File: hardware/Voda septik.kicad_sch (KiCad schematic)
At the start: 40 parts, among them J1 Screw_Terminal_01x09, J3 Display TM1637, J4 Display LCD I2C, J6 Screw_Terminal_01x09, U1 ESP32-DevKitC, U2 DC-DC 24V -> 5V, U3 ADS1115IDGS, U4 MAX3485-modul

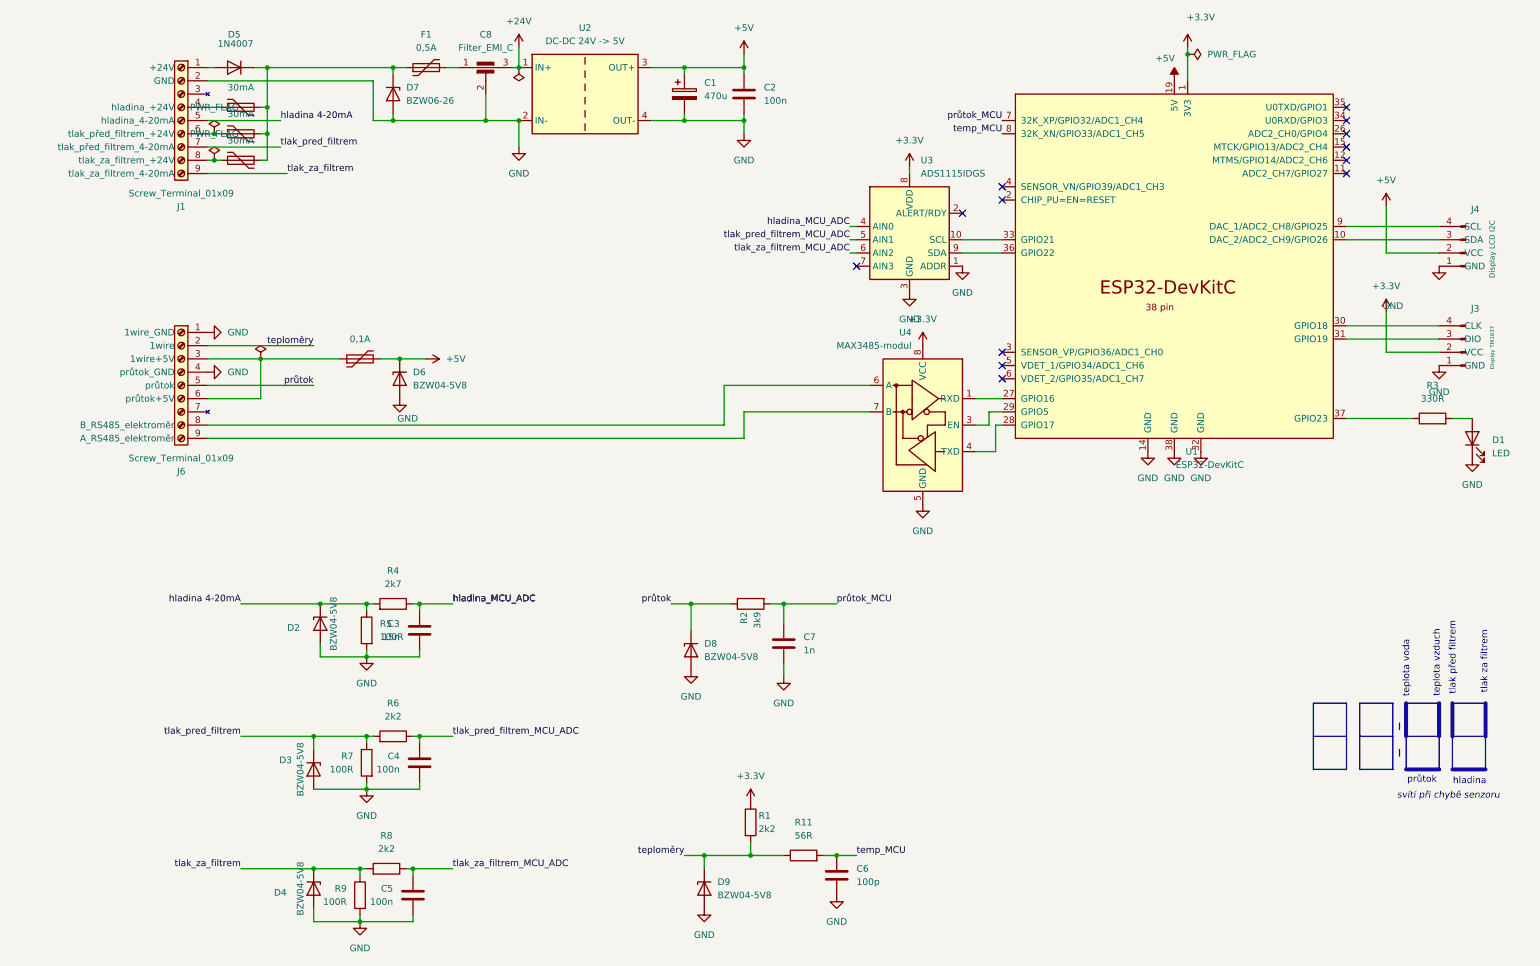
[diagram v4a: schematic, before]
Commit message: Vyvéjíme PCB a jsme v v koncích díky malé krabičce.
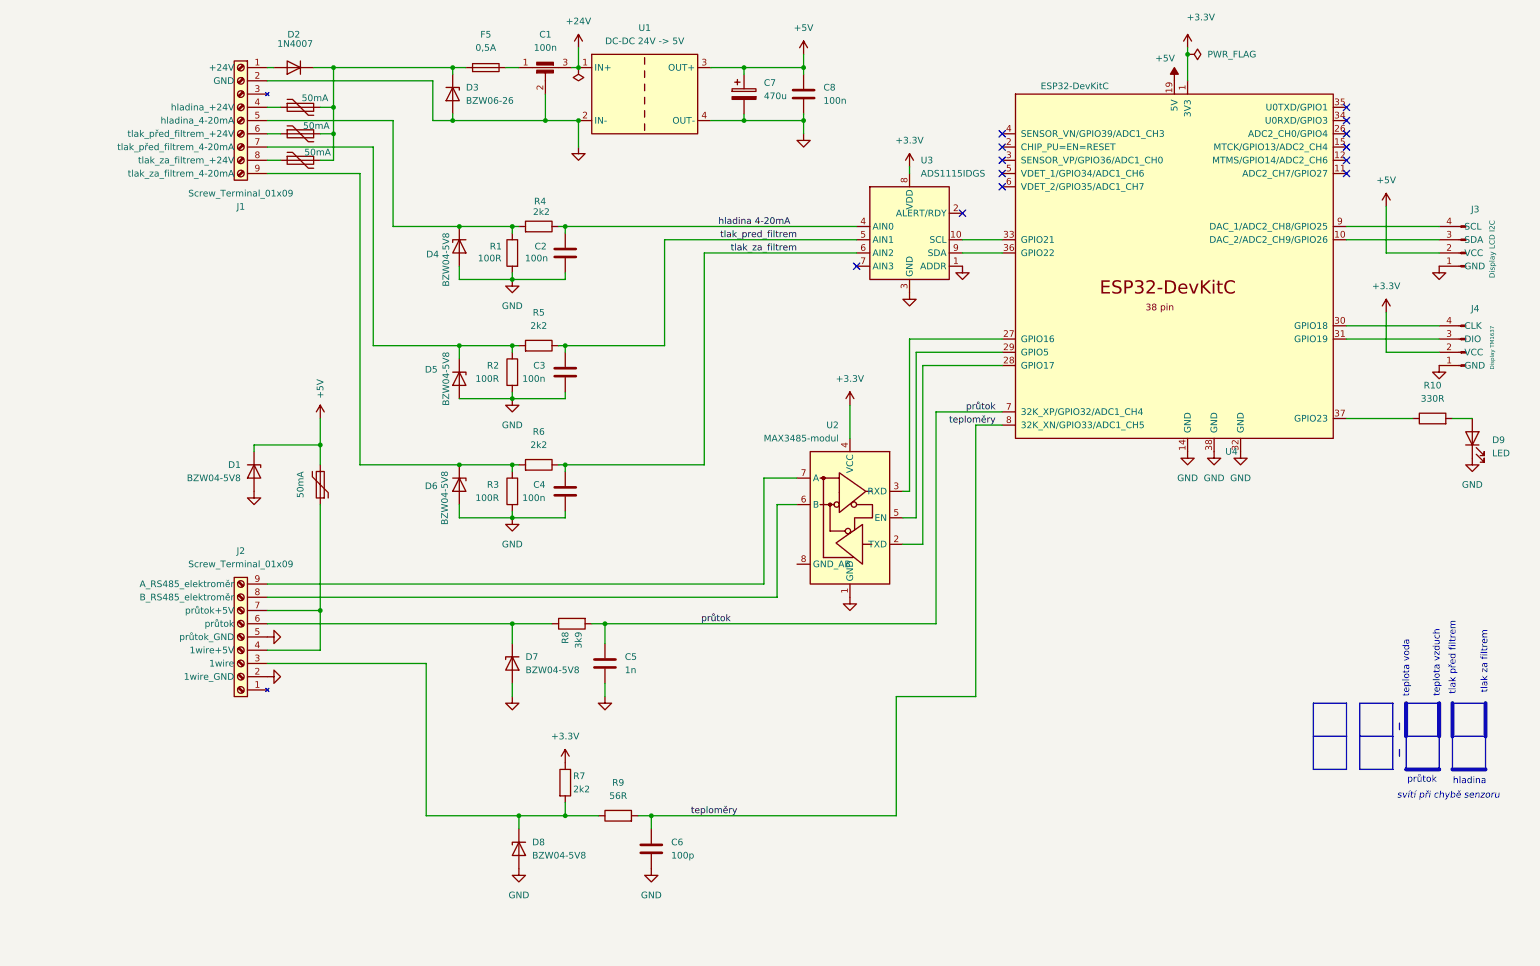
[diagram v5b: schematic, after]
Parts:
- C1: renamed from C8; value Filter_EMI_C -> 100n; footprint (none) -> martin:Odruseni_3x_2.54mm
- C2: renamed from C3; value 15n -> 100n; footprint (none) -> Capacitor_THT:C_Disc_D5.0mm_W2.5mm_P5.00mm
- C3: renamed from C4; footprint (none) -> Capacitor_THT:C_Disc_D5.0mm_W2.5mm_P5.00mm
- C4: renamed from C5; footprint (none) -> Capacitor_THT:C_Disc_D5.0mm_W2.5mm_P5.00mm
- C5: renamed from C7; footprint (none) -> Capacitor_THT:C_Disc_D5.0mm_W2.5mm_P5.00mm
- C6: footprint (none) -> Capacitor_THT:C_Disc_D5.0mm_W2.5mm_P5.00mm
- C7: renamed from C1; footprint (none) -> Capacitor_THT:CP_Radial_D10.0mm_P5.00mm
- C8: renamed from C2; footprint (none) -> Capacitor_THT:C_Disc_D5.0mm_W2.5mm_P5.00mm
- D9: renamed from D1; footprint (none) -> LED_THT:LED_D3.0mm
- F1: renamed from F2; value 30mA -> 50mA; footprint (none) -> martin:Fuse_Disc_D8.3_W3.8_P5.1
- F2: renamed from F3; value 30mA -> 50mA; footprint (none) -> martin:Fuse_Disc_D8.3_W3.8_P5.1
- F3: renamed from F4; value 30mA -> 50mA; footprint (none) -> martin:Fuse_Disc_D8.3_W3.8_P5.1
- F4: renamed from F5; value 0,1A -> 50mA; footprint (none) -> martin:Fuse_Disc_D8.3_W3.8_P5.1
- F5: renamed from F1; footprint (none) -> martin:Fuse_Axial_L11mm_D3.9mm_P15.24mm_Horizontal
- J1: footprint TerminalBlock:TerminalBlock_Xinya_XY308-2.54-9P_1x09_P2.54mm_Horizontal -> martin:Svorky_EB147A_9_5.08
- J2: renamed from J6; footprint TerminalBlock_Phoenix:TerminalBlock_Phoenix_MKDS-1,5-9_1x09_P5.00mm_Horizontal -> martin:Svorky_EB147A_9_5.08
- J3: renamed from J4; footprint (none) -> Connector_PinHeader_2.54mm:PinHeader_1x04_P2.54mm_Vertical
- J4: renamed from J3; footprint (none) -> Connector_PinHeader_2.54mm:PinHeader_1x04_P2.54mm_Vertical
- R1: renamed from R5; footprint (none) -> Resistor_THT:R_Axial_DIN0207_L6.3mm_D2.5mm_P2.54mm_Vertical
- R10: renamed from R3; footprint (none) -> Resistor_THT:R_Axial_DIN0207_L6.3mm_D2.5mm_P2.54mm_Vertical
- R2: renamed from R7; footprint (none) -> Resistor_THT:R_Axial_DIN0207_L6.3mm_D2.5mm_P2.54mm_Vertical
- R3: renamed from R9; footprint (none) -> Resistor_THT:R_Axial_DIN0207_L6.3mm_D2.5mm_P2.54mm_Vertical
- R4: value 2k7 -> 2k2; footprint (none) -> Resistor_THT:R_Axial_DIN0207_L6.3mm_D2.5mm_P2.54mm_Vertical
- R5: renamed from R6; footprint (none) -> Resistor_THT:R_Axial_DIN0207_L6.3mm_D2.5mm_P2.54mm_Vertical
- R6: renamed from R8; footprint (none) -> Resistor_THT:R_Axial_DIN0207_L6.3mm_D2.5mm_P2.54mm_Vertical
- R7: renamed from R1; footprint (none) -> Resistor_THT:R_Axial_DIN0207_L6.3mm_D2.5mm_P2.54mm_Vertical
- R8: renamed from R2; footprint (none) -> Resistor_THT:R_Axial_DIN0207_L6.3mm_D2.5mm_P2.54mm_Vertical
- R9: renamed from R11; footprint (none) -> Resistor_THT:R_Axial_DIN0207_L6.3mm_D2.5mm_P2.54mm_Vertical
- U1: renamed from U2; footprint Converter_DCDC:Converter_DCDC_Murata_CRE1xxxxxxDC_THT -> martin:LM2596 DC-DC HW-411
- U2: renamed from U4; footprint (none) -> martin:MAX3485-modul
- U3: footprint Package_SO:TSSOP-10_3x3mm_P0.5mm -> martin:ADS1115_modul
- renumbered D6 to D1, D5 to D2, D7 to D3, D2 to D4, D3 to D5, D4 to D6, D8 to D7, D9 to D8, U1 to U4
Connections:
- net hladina_MCU_ADC is gone; now on net hladina 4-20mA: C2.1, R4.1, U3.4 (AIN0)
- net průtok_MCU is gone; now on net průtok: C5.1, R8.2, U4.7 (32K_XP/GPIO32/ADC1_CH4)
- net temp_MCU is gone; now on net teploměry: C6.1, R9.2, U4.8 (32K_XN/GPIO33/ADC1_CH5)
- net tlak_pred_filtrem_MCU_ADC is gone; now on net tlak_pred_filtrem: C3.1, R5.1, U3.5 (AIN1)
- net tlak_za_filtrem_MCU_ADC is gone; now on net tlak_za_filtrem: C4.1, R6.1, U3.6 (AIN2)
- net +3.3V: now also U2.4 (VCC); no longer U2.8 (VCC)
- net GND: now also J2.2 (1wire_GND), J2.5 (průtok_GND), U2.1 (GND); no longer J2.1 (1wire_GND), J2.4 (průtok_GND), U2.5 (GND)
- net hladina 4-20mA: no longer D4.1 (K), J1.5 (hladina_4-20mA), R1.1, R4.2
- net průtok: no longer D7.1 (K), J2.5 (průtok), R8.1
- net teploměry: no longer D8.1 (K), J2.2 (1wire), R7.2, R9.1
- net tlak_pred_filtrem: no longer D5.1 (K), J1.7 (tlak_před_filtrem_4-20mA), R2.1, R5.2
- net tlak_za_filtrem: no longer D6.1 (K), J1.9 (tlak_za_filtrem_4-20mA), R3.1, R6.2
- net at U4.27 (GPIO16): now also U2.3 (RXD); no longer U2.1 (RXD)
- net at U4.29 (GPIO5): now also U2.5 (EN); no longer U2.3 (EN)
- net at U4.28 (GPIO17): now also U2.2 (TXD); no longer U2.4 (TXD)
- net at J2.7 (průtok+5V): now also F4.1, J2.4 (1wire+5V)
- new net: D8.1 (K), J2.3 (1wire), R7.2, R9.1
- new net: D5.1 (K), J1.7 (tlak_před_filtrem_4-20mA), R2.1, R5.2
- new net: D7.1 (K), J2.6 (průtok), R8.1
- new net: D4.1 (K), J1.5 (hladina_4-20mA), R1.1, R4.2
- new net: D6.1 (K), J1.9 (tlak_za_filtrem_4-20mA), R3.1, R6.2
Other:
- moved on the sheet: C1, C2, C3, C4, C5, C6, C7, C8, D1, D2, D3, D4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

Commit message: Tak už to mám všechno naroutováno
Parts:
- added U5: CA56-12CGKWA, martin:DISPLAY_clok_MOUNT_4xM3, symbol Display_Character:CA56-12CGKWA
- D1, D3, D4, D5, D6, D7, D8: footprint Diode_THT:D_DO-15_P10.16mm_Horizontal -> Diode_THT:D_DO-15_P2.54mm_Vertical_AnodeUp
- D2: footprint Diode_THT:D_DO-41_SOD81_P10.16mm_Horizontal -> Diode_THT:D_DO-15_P2.54mm_Vertical_AnodeUp
- J1: value Screw_Terminal_01x09 -> Napájení a 4-20mA senzory; footprint martin:Svorky_EB147A_9_5.08 -> martin:Svorky_EB147A_8_5.08
- J2: footprint martin:Svorky_EB147A_9_5.08 -> martin:Svorky_EB147A_8_5.08
- U3: footprint martin:ADS1115_modul -> martin:ADS1115_modul_vertical
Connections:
- net +3.3V: now also U3.1 (VDD); no longer U3.8 (VDD)
- net GND: now also J2.3 (1wire_GND), J2.6 (průtok_GND), U3.2 (GND), U3.5 (ADDR); no longer J2.2 (1wire_GND), J2.5 (průtok_GND), U3.1 (ADDR), U3.3 (GND)
- net hladina 4-20mA: now also U3.10 (AIN3); no longer U3.4 (AIN0)
- net průtok: now also U4.8 (32K_XN/GPIO33/ADC1_CH5); no longer U4.7 (32K_XP/GPIO32/ADC1_CH4)
- net teploměry: now also U4.7 (32K_XP/GPIO32/ADC1_CH4); no longer U4.8 (32K_XN/GPIO33/ADC1_CH5)
- net tlak_pred_filtrem: no longer C3.1, R5.1, U3.5 (AIN1)
- net tlak_za_filtrem: now also U3.8 (AIN1); no longer U3.6 (AIN2)
- net at D8.1 (K), R7.2, R9.1: now also J2.4 (1wire); no longer J2.3 (1wire)
- net at D5.1 (K), R2.1, R5.2: now also J1.6 (tlak_před_filtrem_4-20mA); no longer J1.7 (tlak_před_filtrem_4-20mA)
- net at F2.1: now also J1.5 (tlak_před_filtrem_+24V); no longer J1.6 (tlak_před_filtrem_+24V)
- net at D7.1 (K), R8.1: now also J2.7 (průtok); no longer J2.6 (průtok)
- net at R10.1: now also U4.27 (GPIO16); no longer U4.37 (GPIO23)
- net at D4.1 (K), R1.1, R4.2: now also J1.4 (hladina_4-20mA); no longer J1.5 (hladina_4-20mA)
- net at J4.3 (DIO): now also U4.30 (GPIO18); no longer U4.31 (GPIO19)
- net at J4.4 (CLK): now also U4.28 (GPIO17); no longer U4.30 (GPIO18)
- net at U2.2 (TXD): now also U4.11 (ADC2_CH7/GPIO27); no longer U4.28 (GPIO17)
- net at U2.3 (RXD): now also U4.10 (DAC_2/ADC2_CH9/GPIO26); no longer U4.27 (GPIO16)
- net at U2.5 (EN): now also U4.9 (DAC_1/ADC2_CH8/GPIO25); no longer U4.29 (GPIO5)
- net at U2.6 (B): now also J2.2 (B_RS485_elektroměr); no longer J2.8 (B_RS485_elektroměr)
- net at U2.7 (A): now also J2.1 (A_RS485_elektroměr); no longer J2.9 (A_RS485_elektroměr)
- net at F3.1: now also J1.7 (tlak_za_filtrem_+24V); no longer J1.8 (tlak_za_filtrem_+24V)
- net at J3.3 (SDA): now also U4.36 (GPIO22); no longer U4.10 (DAC_2/ADC2_CH9/GPIO26)
- net at U4.12 (MTMS/GPIO14/ADC2_CH6): now also U3.4 (SDA)
- net at U4.15 (MTCK/GPIO13/ADC2_CH4): now also U3.3 (SCL)
- net at U4.33 (GPIO21): no longer U3.10 (SCL)
- net at U3.9 (AIN2): now also C3.1, R5.1; no longer U4.36 (GPIO22)
- net at J3.4 (SCL): now also U4.37 (GPIO23); no longer U4.9 (DAC_1/ADC2_CH8/GPIO25)
- net at D6.1 (K), R3.1, R6.2: now also J1.8 (tlak_za_filtrem_4-20mA); no longer J1.9 (tlak_za_filtrem_4-20mA)
- net at F1.1: now also J1.3 (hladina_+24V); no longer J1.4 (hladina_+24V)
- new net: F4.1, J2.5 (1wire+5V), J2.8 (průtok+5V)
- no-connect marks 13 -> 14

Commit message: Hotový návrh desky a schématu, které jdou do výroby.
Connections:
- net tlak_pred_filtrem: now also C3.1, R5.1, U3.9 (AIN2)
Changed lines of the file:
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@@
 	)
 	(label "tlak_pred_filtrem"
-		(at 147.32 55.88 180)
+		(at 143.51 58.42 180)
 		(effects
 			(font
